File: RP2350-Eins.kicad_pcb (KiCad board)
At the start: 4 copper layers, 68.6 x 53.3 mm, 66 parts, among them J1 CONN_PWR, J10 CONN_USB, J2 CONN_ICSP, J3 CONN_A, J4 CONN_P, J5 CONN_X, J6 CONN_DBG, J7 CONN_JTAG, J8 CONN_D1, J9 CONN_D2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

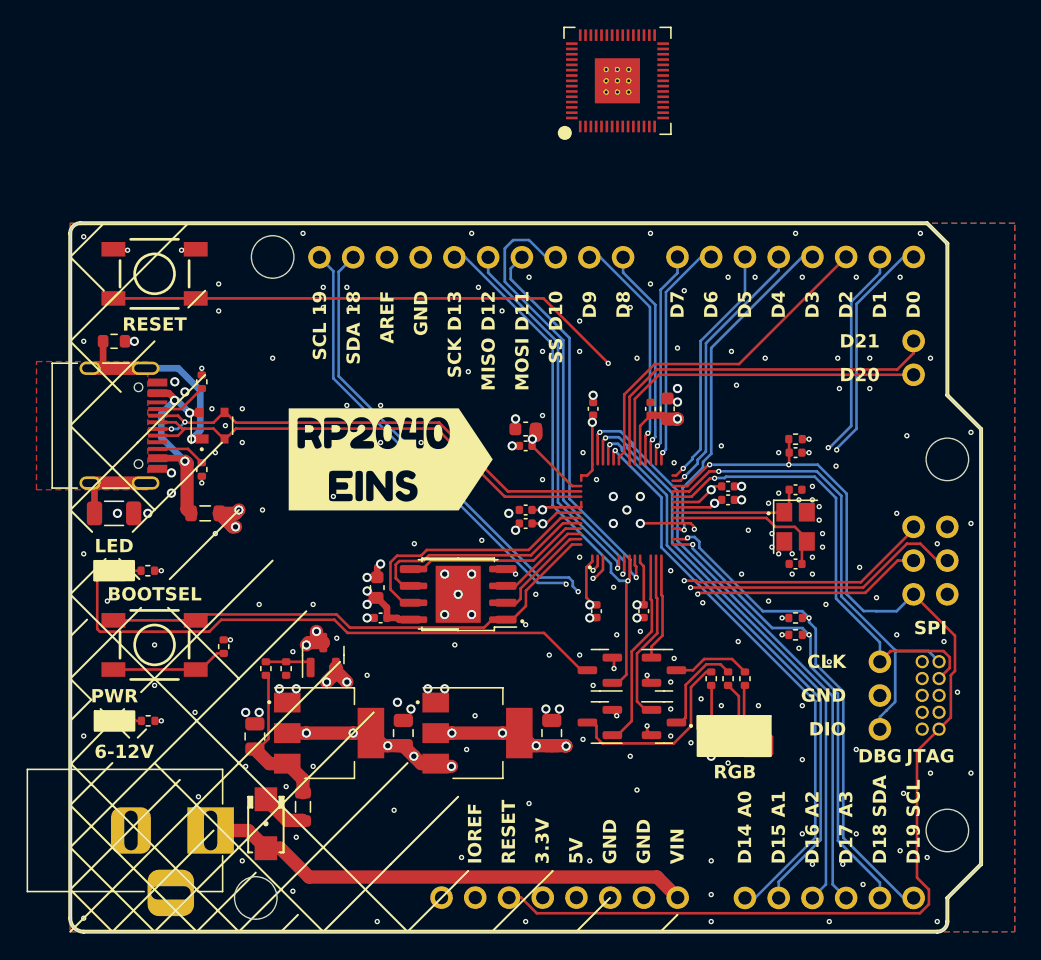
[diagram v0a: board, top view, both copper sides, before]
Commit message: Added missing components. Routed the board.
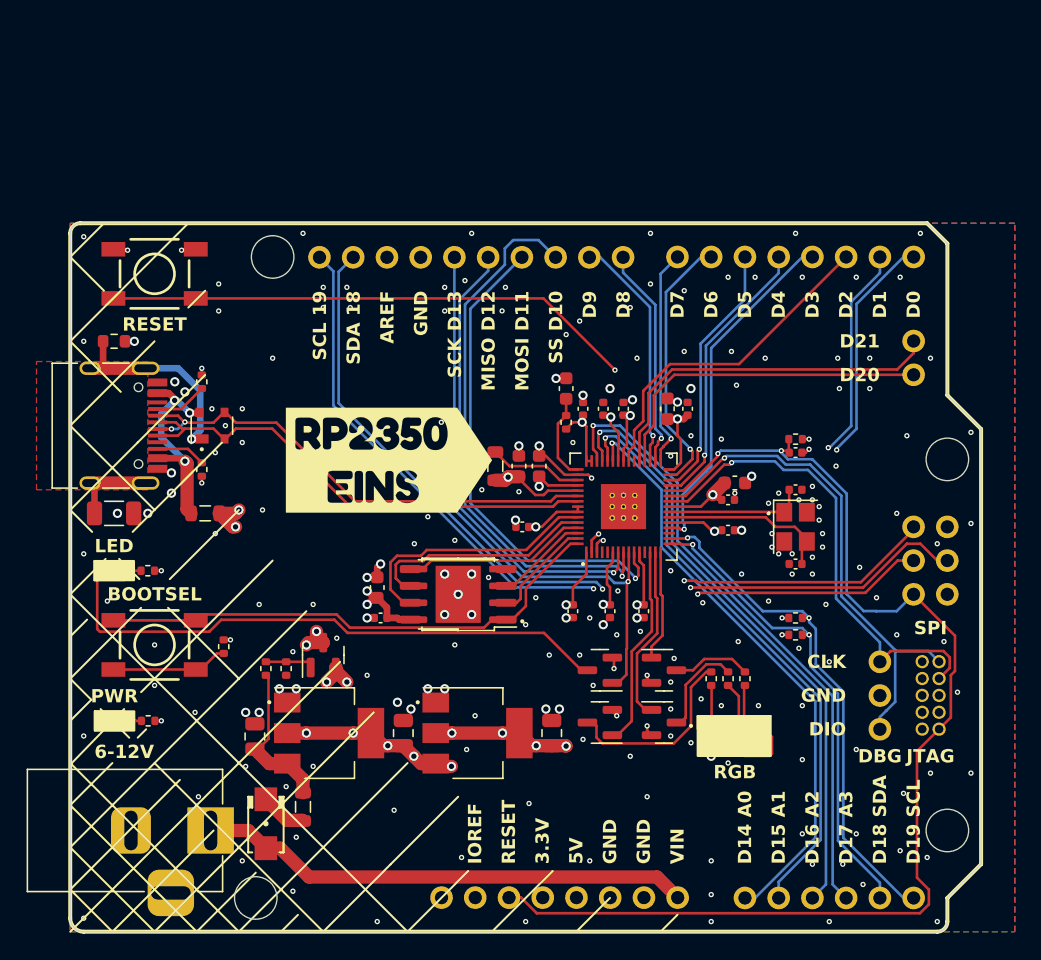
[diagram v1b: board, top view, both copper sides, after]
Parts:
- added C17: 2.2uF, Capacitor_SMD:C_0603_1608Metric, F.Cu at (160.8, 91.9)
- added C18: 2.2uF, Capacitor_SMD:C_0603_1608Metric, F.Cu at (162.3, 91.9)
- added C23: 2.2uF, Capacitor_SMD:C_0603_1608Metric, F.Cu at (164.3, 86.1)
- added C24: 100nF, Capacitor_SMD:C_0402_1005Metric, F.Cu at (168.7, 87.6)
- added L1: 3.3uH, Inductor_SMD:L_0805_2012Metric, F.Cu at (159.0, 91.9)
- added R2: 33, Resistor_SMD:R_0402_1005Metric, F.Cu at (164.3, 88.6)
- G2: value BOARD-LABEL -> G***; footprint kibuzzard-654A67CC -> kibuzzard-66CA2205
- moved U2 32.1 mm to (168.7, 95.0)
- moved C5 16.3 mm to (177.0, 93.2), turned to 0 degrees
- moved C22 9.16 mm to (167.6, 102.9), turned to -90 degrees
- moved C9 6.48 mm to (167.1, 87.6), turned to 90 degrees
- moved C3 2.79 mm to (173.5, 87.6)
- moved C6 2.29 mm to (176.5, 96.8)
- moved C11 1.78 mm to (164.8, 102.9)
- moved C10 1.30 mm to (161.0, 96.5)
- moved C7 1.02 mm to (176.5, 94.5)
- moved C4 0.76 mm to (165.6, 87.6)
- moved G2 0.14 mm to (151.0, 91.5)
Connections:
- U2 pad 1: unconnected-(U2-IOVDD-Pad1) -> +3V3
- U2 pad 11: unconnected-(U2-IOVDD-Pad11) -> +3V3
- U2 pad 20: unconnected-(U2-IOVDD-Pad20) -> +3V3
- U2 pad 23: unconnected-(U2-DVDD-Pad23) -> +1V1
- U2 pad 30: unconnected-(U2-IOVDD-Pad30) -> +3V3
- U2 pad 38: unconnected-(U2-IOVDD-Pad38) -> +3V3
- U2 pad 39: unconnected-(U2-DVDD-Pad39) -> +1V1
- U2 pad 44: unconnected-(U2-ADC_AVDD-Pad44) -> +3V3
- U2 pad 45: unconnected-(U2-IOVDD-Pad45) -> +3V3
- U2 pad 46: unconnected-(U2-VREG_AVDD-Pad46) -> VREG_AVDD
- U2 pad 47: unconnected-(U2-VREG_PGND-Pad47) -> GND
- U2 pad 48: unconnected-(U2-VREG_LX-Pad48) -> VREG_LX
- U2 pad 49: unconnected-(U2-VREG_VIN-Pad49) -> +3V3
- U2 pad 50: unconnected-(U2-VREG_FB-Pad50) -> +1V1
- U2 pad 53: unconnected-(U2-USB_OTP_VDD-Pad53) -> +3V3
- U2 pad 54: unconnected-(U2-QSPI_IOVDD-Pad54) -> +3V3
- U2 pad 55: unconnected-(U2-QSPI_SD3-Pad55) -> QSPI_SD3
- U2 pad 57: unconnected-(U2-QSPI_SD0-Pad57) -> QSPI_SD0
- U2 pad 58: unconnected-(U2-QSPI_SD2-Pad58) -> QSPI_SD2
- U2 pad 59: unconnected-(U2-QSPI_SD1-Pad59) -> QSPI_SD1
- U2 pad 6: unconnected-(U2-DVDD-Pad6) -> +1V1
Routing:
- net +1V1: track 35.0 -> 53.8 mm, vias 3 -> 4
- net +3V3: track 48.2 -> 58.2 mm, vias 18 -> 20
- net D11_MOSI: track 55.7 -> 62.8 mm
- net VREG_LX: track 0.00 -> 7.09 mm
- net D12_MISO: track 53.0 -> 60.1 mm
- net D10_SS: track 34.3 -> 41.3 mm
- net VREG_AVDD: track 0.00 -> 6.56 mm
- net D13_SCK: track 64.0 -> 67.9 mm
- net D0_RX: track 42.4 -> 39.0 mm
- net D6: track 17.6 -> 20.1 mm
- net D19_SCL: track 83.2 -> 84.9 mm
- net D1_TX: track 39.4 -> 37.8 mm
- net SWD: track 37.5 -> 38.9 mm
- net SWCLK: track 35.0 -> 36.4 mm
- net D18_SDA: track 80.9 -> 82.2 mm
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
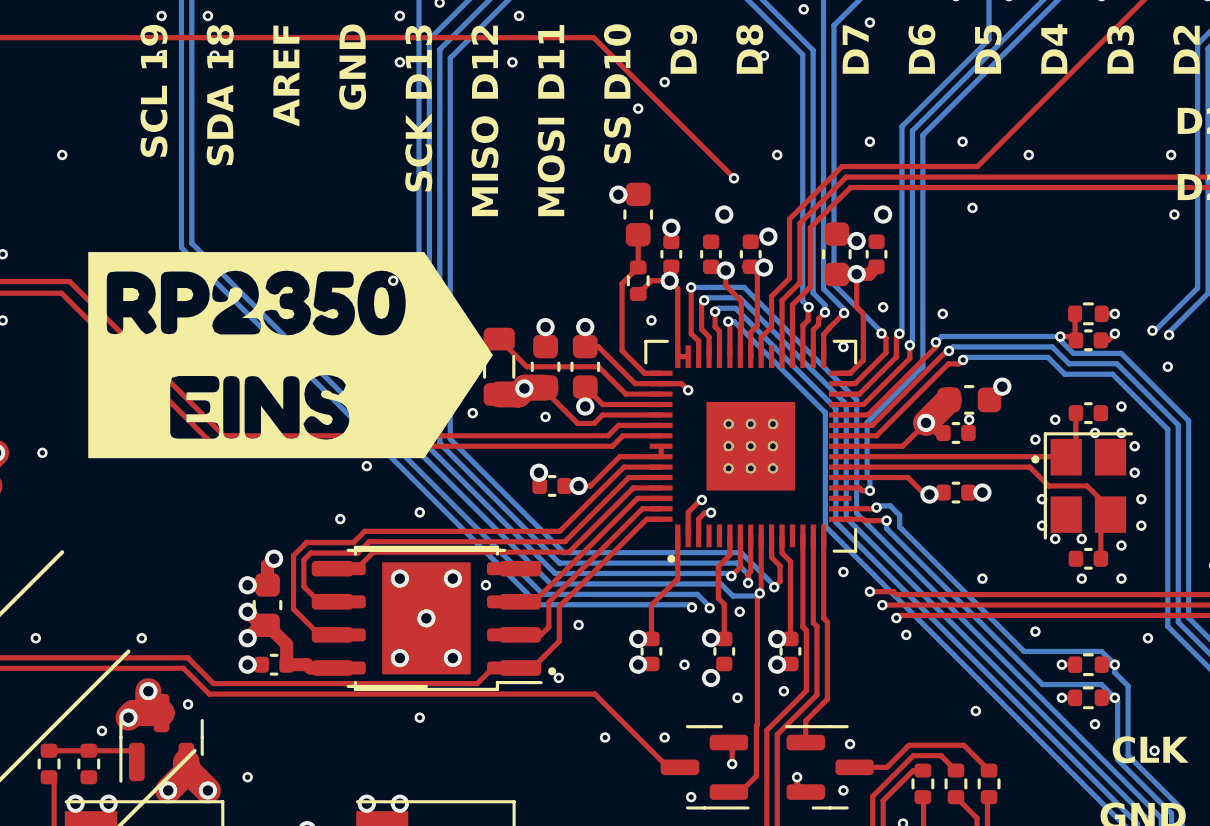
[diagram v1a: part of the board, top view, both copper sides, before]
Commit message: Added few vias. Moved staff around.
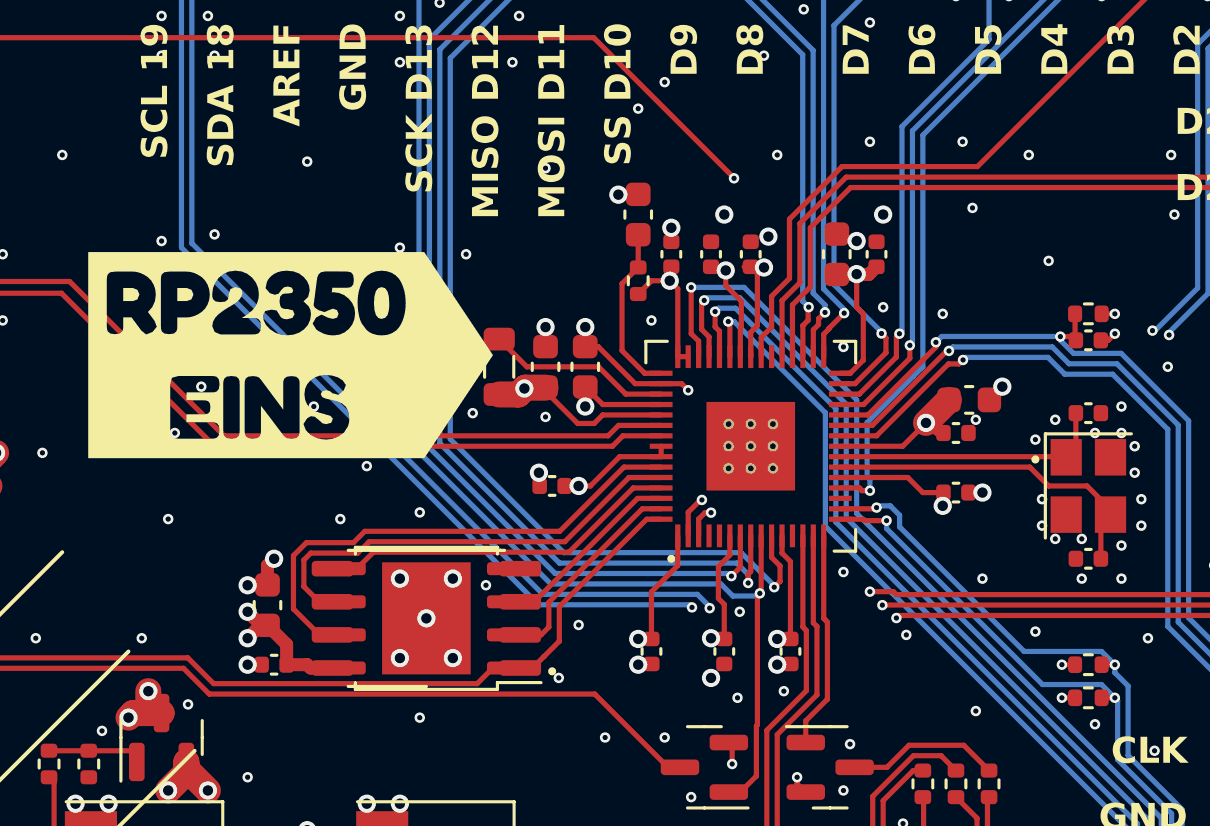
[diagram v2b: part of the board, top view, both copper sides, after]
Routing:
- net GND: vias 213 -> 221
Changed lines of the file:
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@@
 		(tags "capacitor")
 		(property "Reference" "C5"
-			(at 0 -1.43 360)
+			(at 0 -1.43 0)
 			(layer "F.SilkS")
 			(hide yes)
@@
 		)
 		(property "Value" "2.2uF"
-			(at 0 1.43 360)
+			(at 0 1.43 0)
 			(layer "F.Fab")
 			(effects
@@
 		)
 		(property "Footprint" "Capacitor_SMD:C_0603_1608Metric"
-			(at 0 0 360)
+			(at 0 0 0)
 			(layer "F.Fab")
 			(hide yes)
@@
 		)
 		(property "Datasheet" ""
-			(at 0 0 360)
+			(at 0 0 0)
 			(layer "F.Fab")
 			(hide yes)
@@
 		)
 		(property "Description" ""
-			(at 0 0 360)
+			(at 0 0 0)
 			(layer "F.Fab")
 			(hide yes)
@@
 		)
 		(fp_text user "${REFERENCE}"
-			(at 0 0 360)
+			(at 0 0 0)
 			(layer "F.Fab")
 			(effects
@@
 				(font
 					(size 0.001 0.001)
+					(thickness 0.15)
 				)
 			)
@@
 				(font
 					(size 0.001 0.001)
+					(thickness 0.15)
 				)
 			)
@@
 	)
 	(segment
-		(start 172.0935 96.196)
-		(end 174.682 96.196)
-		(width 0.2)
-		(layer "F.Cu")
-		(net 1)
-	)
-	(segment
 		(start 168.656 91.5585)
 		(end 168.656 90.621186)
@@
 	)
 	(segment
-		(start 174.682 96.196)
-		(end 175.26 96.774)
-		(width 0.2)
-		(layer "F.Cu")
-		(net 1)
-	)
-	(segment
 		(start 162.085 112.997)
 		(end 161.765 112.997)
@@
 	)
 	(segment
+		(start 165.856 99.574)
+		(end 165.856 98.4335)
+		(width 0.2)
+		(layer "F.Cu")
+		(net 1)
+	)
+	(segment
 		(start 162.052 96.52)
 		(end 161.516 96.52)
@@
 	)
 	(segment
-		(start 165.856 100.082)
-		(end 165.856 98.4335)
+		(start 175.26 96.774)
+		(end 176.05 96.774)
 		(width 0.2)
 		(layer "F.Cu")
@@
 	)
 	(segment
-		(start 164.846 101.092)
-		(end 165.856 100.082)
-		(width 0.2)
-		(layer "F.Cu")
-		(net 1)
-	)
-	(segment
 		(start 173.187 88.405)
 		(end 173.482 88.11)
@@
 	)
 	(segment
+		(start 164.846 100.584)
+		(end 165.856 99.574)
+		(width 0.2)
+		(layer "F.Cu")
+		(net 1)
+	)
+	(segment
 		(start 162.502314 96.52)
 		(end 163.626314 95.396)
@@
 	)
 	(segment
+		(start 172.0935 96.196)
+		(end 174.682 96.196)
+		(width 0.2)
+		(layer "F.Cu")
+		(net 1)
+	)
+	(segment
 		(start 172.472 92.196)
 		(end 172.0935 92.196)
@@
 	)
 	(segment
+		(start 164.846 102.39)
+		(end 164.846 100.584)
+		(width 0.2)
+		(layer "F.Cu")
+		(net 1)
+	)
+	(segment
 		(start 172.974 91.694)
 		(end 172.472 92.196)
@@
 	)
 	(segment
-		(start 175.26 96.774)
-		(end 176.05 96.774)
-		(width 0.2)
+		(start 152.61 103.505)
+		(end 151.765 103.505)
+		(width 0.5)
 		(layer "F.Cu")
 		(net 1)
 	)
 	(segment
-		(start 152.61 103.505)
-		(end 151.765 103.505)
-		(width 0.5)
+		(start 174.682 96.196)
+		(end 175.26 96.774)
+		(width 0.2)
 		(layer "F.Cu")
 		(net 1)
@@
 	)
 	(segment
-		(start 164.846 102.39)
-		(end 164.846 101.092)
-		(width 0.2)
-		(layer "F.Cu")
-		(net 1)
-	)
-	(segment
 		(start 165.2185 93.396)
 		(end 162.979 93.396)
@@
 	)
 	(via
-		(at 175.514 96.850889)
+		(at 176.022 97.282)
 		(size 0.7)
 		(drill 0.4)
@@
 	)
 	(via
-		(at 154.94 88.646)
+		(at 155.194 87.376)
 		(size 0.4)
 		(drill 0.2)
@@
 	)
 	(via
+		(at 160.782 84.328)
+		(size 0.4)
+		(drill 0.2)
+		(layers "F.Cu" "B.Cu")
+		(free yes)
+		(net 4)
+	)
+	(via
 		(at 173.736 86.106)
 		(size 0.7)
@@
 	)
 	(via
+		(at 157.734 87.63)
+		(size 0.4)
+		(drill 0.2)
+		(layers "F.Cu" "B.Cu")
+		(free yes)
+		(net 4)
+	)
+	(via
 		(at 172.466 106.426)
 		(size 0.4)
@@
 	)
 	(via
+		(at 146.558 94.488)
+		(size 0.4)
+		(drill 0.2)
+		(layers "F.Cu" "B.Cu")
+		(free yes)
+		(net 4)
+	)
+	(via
+		(at 148.082 86.868)
+		(size 0.4)
+		(drill 0.2)
+		(layers "F.Cu" "B.Cu")
+		(free yes)
+		(net 4)
+	)
+	(via
 		(at 177.546 100.076)
 		(size 0.4)
@@
 	)
 	(via
-		(at 152.4 93.98)
+		(at 151.892 93.472)
 		(size 0.4)
 		(drill 0.2)
@@
 	)
 	(via
-		(at 177.038 93.98)
+		(at 177.292 93.98)
 		(size 0.4)
 		(drill 0.2)
@@
 	)
 	(via
+		(at 146.05 87.122)
+		(size 0.4)
+		(drill 0.2)
+		(layers "F.Cu" "B.Cu")
+		(free yes)
+		(net 4)
+	)
+	(via
 		(at 135.636 86.36)
 		(size 0.7)
@@
 	)
 	(via
+		(at 146.304 97.79)
+		(size 0.4)
+		(drill 0.2)
+		(layers "F.Cu" "B.Cu")
+		(free yes)
+		(net 4)
+	)
+	(via
 		(at 147.066 104.902)
 		(size 0.4)
@@
 	)
 	(via
-		(at 166.116 103.378)
-		(size 0.4)
-		(drill 0.2)
-		(layers "F.Cu" "B.Cu")
-		(free yes)
-		(net 4)
-	)
-	(via
 		(at 155.956 97.536)
 		(size 0.4)
@@
 	)
 	(via
+		(at 147.574 92.71)
+		(size 0.4)
+		(drill 0.2)
+		(layers "F.Cu" "B.Cu")
+		(free yes)
+		(net 4)
+	)
+	(via
 		(at 128.016 82.55)
 		(size 0.4)
@@
 	)
 	(via
+		(at 180.086 87.884)
+		(size 0.4)
+		(drill 0.2)
+		(layers "F.Cu" "B.Cu")
+		(free yes)
+		(net 4)
+	)
+	(via
 		(at 140.208 110.49)
 		(size 0.7)
@@
 		(layers "F.Cu" "B.Cu")
 		(free yes)
+		(net 4)
+	)
+	(via
+		(at 151.638 84.074)
+		(size 0.4)
+		(drill 0.2)
+		(layers "F.Cu" "B.Cu")
+		(free yes)

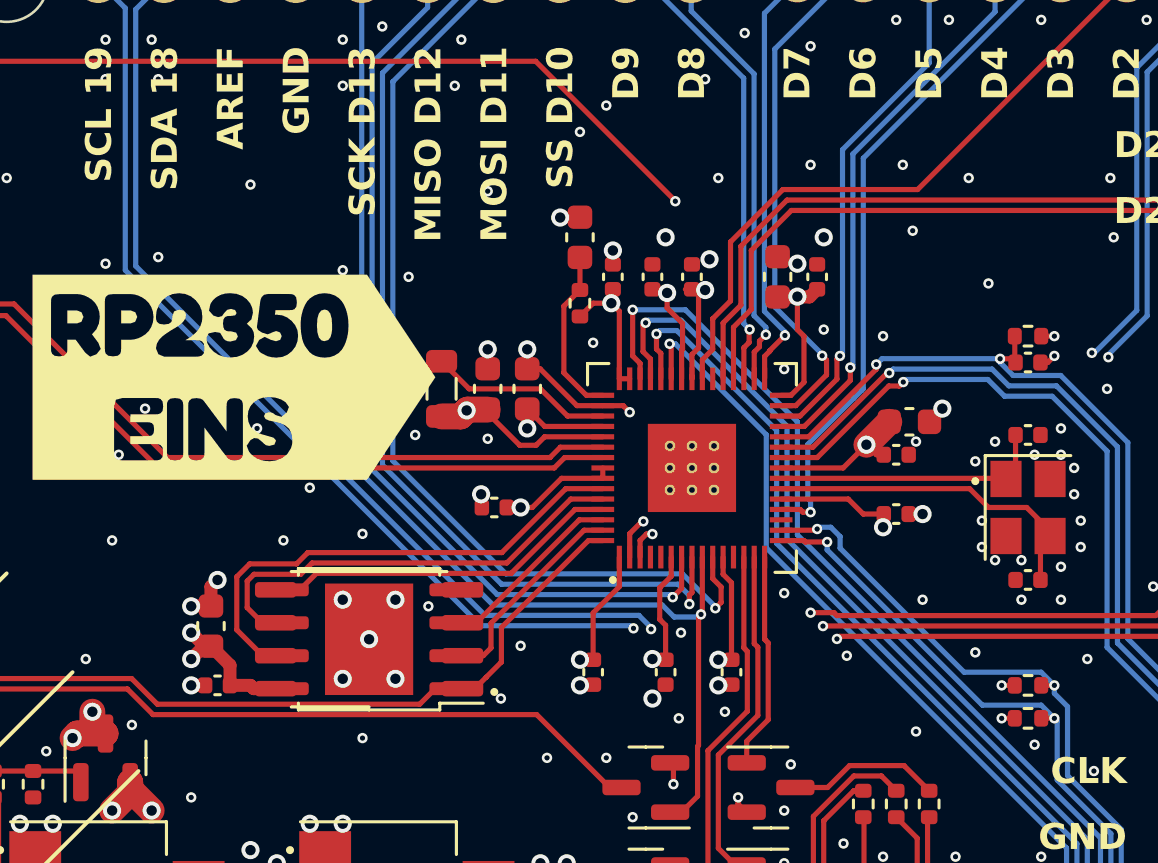
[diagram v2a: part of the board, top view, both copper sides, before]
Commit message: Moved staff around.
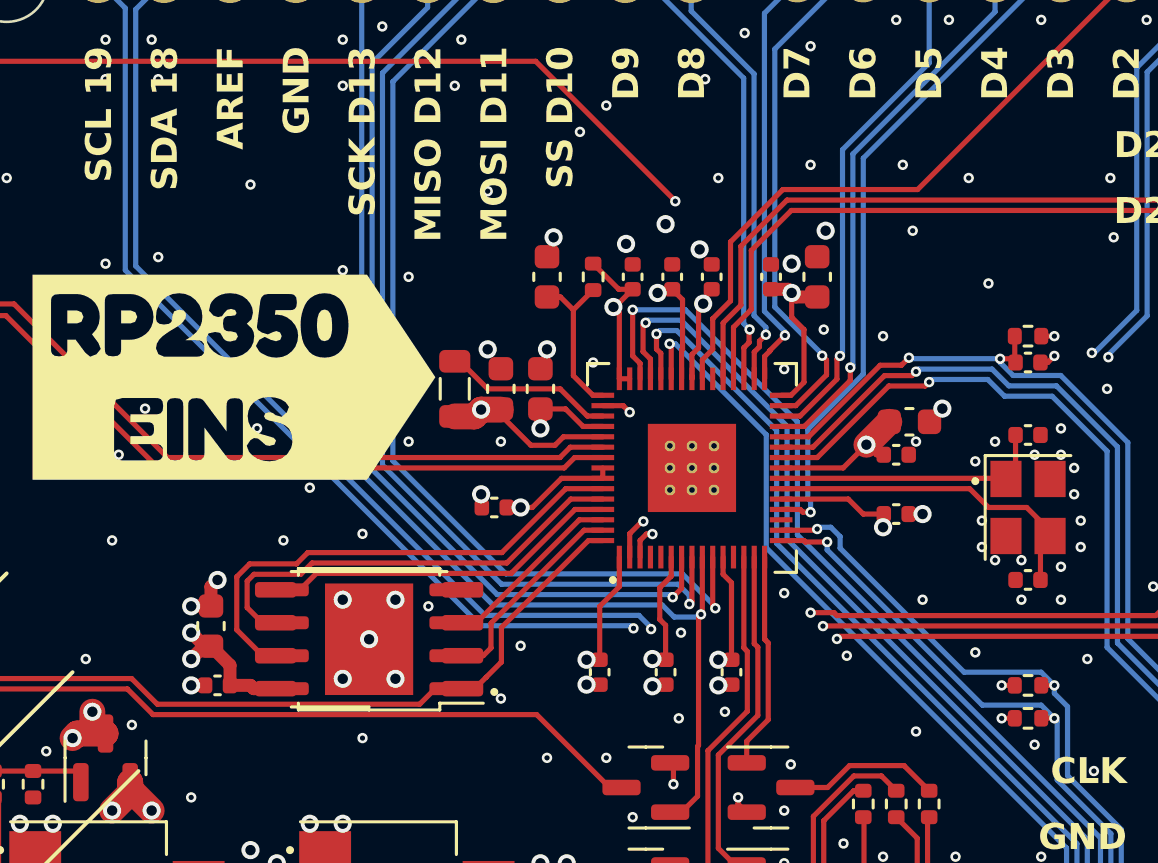
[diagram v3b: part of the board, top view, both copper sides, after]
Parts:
- moved C23 1.98 mm to (163.1, 87.6)
- moved C3 1.78 mm to (171.7, 87.6)
- moved C1 1.52 mm to (173.5, 87.6)
- moved R2 1.14 mm to (164.8, 87.6), turned to -90 degrees
- moved C24 0.76 mm to (169.4, 87.6)
- moved C4 0.76 mm to (166.4, 87.6)
- moved C9 0.76 mm to (167.9, 87.6)
- moved L1 0.51 mm to (159.5, 91.9)
- moved C17 0.51 mm to (161.3, 91.9)
- moved C18 0.51 mm to (162.8, 91.9)
- moved C11 0.25 mm to (165.1, 102.9)
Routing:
- net GND: track 14.9 -> 11.4 mm
- net +3V3: track 58.2 -> 57.0 mm
- net RESET: track 140.2 -> 141.2 mm
- net +1V1: track 53.8 -> 53.0 mm
- net VREG_LX: track 7.09 -> 6.58 mm
